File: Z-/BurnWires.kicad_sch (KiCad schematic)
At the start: 27 parts, among them K1 IM02DGR, Q11 IRLML2803, Q13 IRLML2803, Q15 IRF7404, Q17 IRF7404, Q18 IRLML2803, Q19 IRF7404, Q9 MMBT2222AT

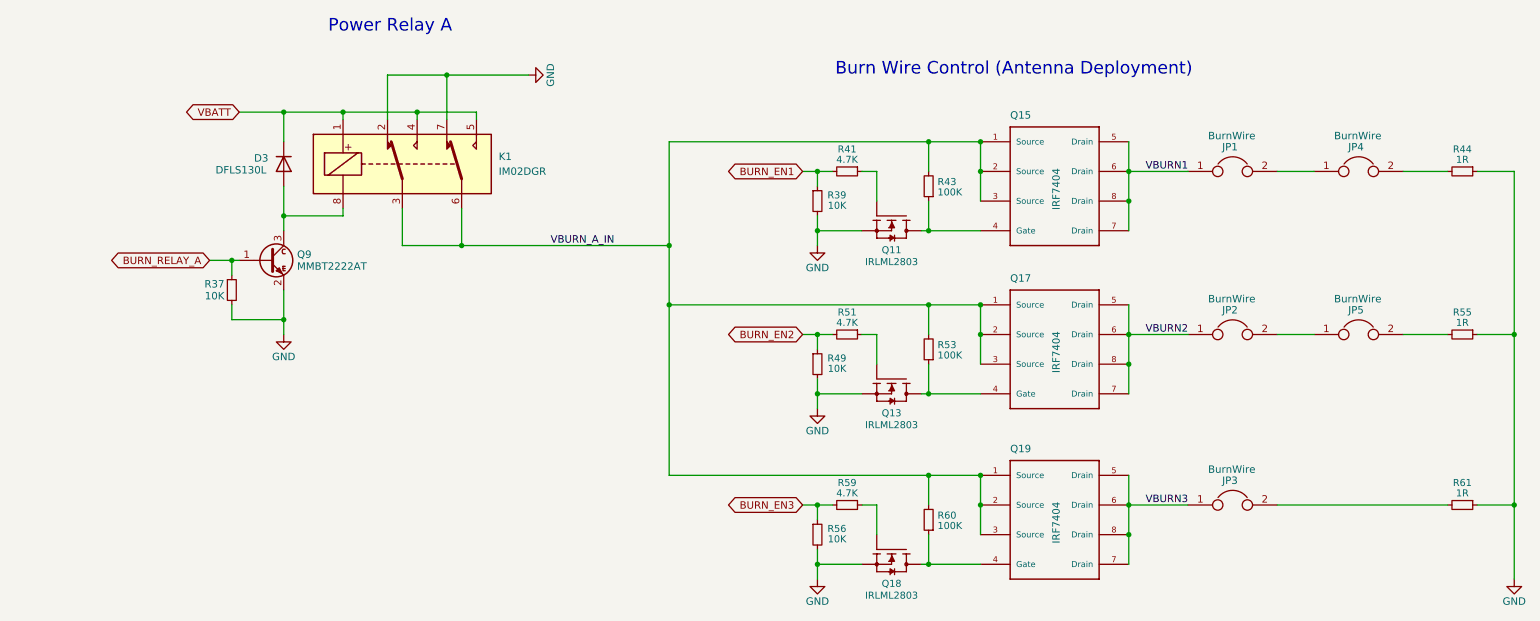
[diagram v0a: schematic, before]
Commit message: Added i2c expander for burnwires, reformatted i2c protection, swapped to drv8235
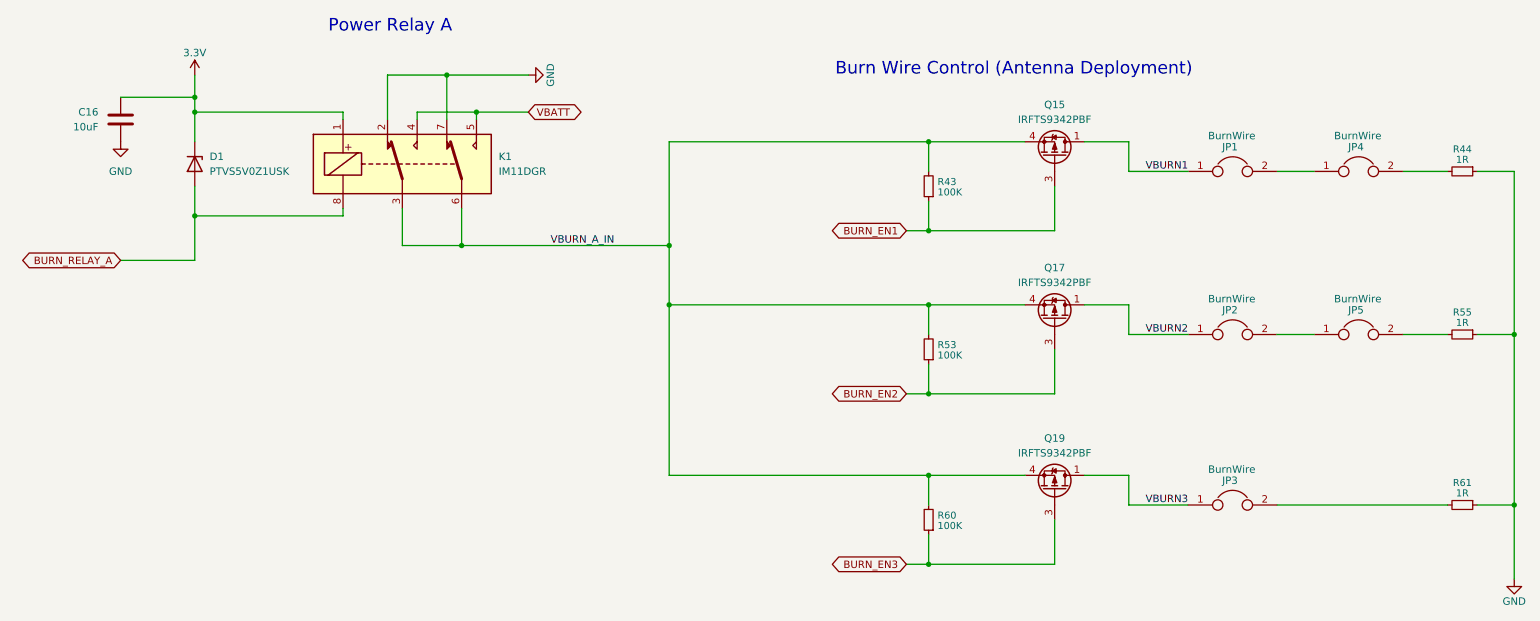
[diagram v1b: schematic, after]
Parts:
- removed D3: DFLS130L, Diode_SMD:D_PowerDI-123, symbol SolarPanels:D
- removed Q11, Q13, Q18: IRLML2803, Package_TO_SOT_SMD:SOT-23, symbol SolarPanels:IRLML2803TRPBF
- removed Q15, Q17, Q19: IRF7404, Package_SO:SOIC-8_3.9x4.9mm_P1.27mm, symbol SolarPanels:NDS8434_3
- removed Q9: MMBT2222AT, Package_TO_SOT_SMD:SOT-23, symbol SolarPanels:MMBT2222AT
- removed R37, R39, R49, R56: 10K, Resistor_SMD:R_0603_1608Metric, symbol SolarPanels:R_Small
- removed R41, R51, R59: 4.7K, Resistor_SMD:R_0603_1608Metric, symbol SolarPanels:R_Small
- added C16: 10uF, Capacitor_SMD:C_1206_3216Metric, symbol Device:C
- added D1: PTVS5V0Z1USK, Diode_SMD:Nexperia_DSN1608-2_1.6x0.8mm, symbol Diode:PTVS5V0Z1USK
- added Q15, Q17, Q19: IRFTS9342PBF, Package_SO:TSOP-6_1.65x3.05mm_P0.95mm, symbol Transistor_FET:IRFTS9342PBF
- K1: value IM02DGR -> IM11DGR
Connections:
- net BURN_EN1: now also R43.1, Q15.3 (G)
- net BURN_EN2: now also R53.1, Q17.3 (G)
- net BURN_EN3: now also R60.1, Q19.3 (G)
- net BURN_RELAY_A: now also K1.8, D1.2 (A)
- net GND: now also C16.2
- net VBATT: no longer K1.1
- net VBURN1: now also Q15.1 (D), Q15.2 (D), Q15.5 (D), Q15.6 (D)
- net VBURN2: now also Q17.1 (D), Q17.2 (D), Q17.5 (D), Q17.6 (D)
- net VBURN3: now also Q19.1 (D), Q19.2 (D), Q19.5 (D), Q19.6 (D)
- net VBURN_A_IN: now also Q15.4 (S), Q17.4 (S), Q19.4 (S)
- new net 3.3V: C16.1, D1.1 (K), K1.1

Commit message: Moved burnwire around and added switch to coil driver
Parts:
- JP1, JP2, JP3, JP4, JP5: footprint SolarPanels:Burn-Wire -> Argus-Miscellaneous:Burn-Wire; symbol SolarPanels:Device_Jumper -> SP:Device_Jumper
- K1: symbol SolarPanels:IM02 -> Relay:IM02
- R43, R44, R53, R55, R60, R61: symbol SolarPanels:R_Small -> Device:R_Small
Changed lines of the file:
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@@
 	)
 	(symbol
-		(lib_id "SolarPanels:R_Small")
+		(lib_id "Device:R_Small")
 		(at 177.8 101.6 180)
 		(unit 1)
@@
 	)
 	(symbol
-		(lib_id "SolarPanels:Device_Jumper")
+		(lib_id "SP:Device_Jumper")
 		(at 251.46 71.12 0)
 		(unit 1)
@@
 			)
 		)
-		(property "Footprint" "SolarPanels:Burn-Wire"
+		(property "Footprint" "Argus-Miscellaneous:Burn-Wire"
 			(at 251.46 71.12 0)
 			(effects
@@
 	)
 	(symbol
-		(lib_id "SolarPanels:Device_Jumper")
+		(lib_id "SP:Device_Jumper")
 		(at 229.87 99.06 0)
 		(unit 1)
@@
 			)
 		)
-		(property "Footprint" "SolarPanels:Burn-Wire"
+		(property "Footprint" "Argus-Miscellaneous:Burn-Wire"
 			(at 229.87 99.06 0)
 			(effects
@@
 	)
 	(symbol
-		(lib_id "SolarPanels:Device_Jumper")
+		(lib_id "SP:Device_Jumper")
 		(at 251.46 99.06 0)
 		(unit 1)
@@
 			)
 		)
-		(property "Footprint" "SolarPanels:Burn-Wire"
+		(property "Footprint" "Argus-Miscellaneous:Burn-Wire"
 			(at 251.46 99.06 0)
 			(effects
@@
 	)
 	(symbol
-		(lib_id "SolarPanels:R_Small")
+		(lib_id "Device:R_Small")
 		(at 269.24 71.12 270)
 		(unit 1)
@@
 	)
 	(symbol
-		(lib_id "SolarPanels:IM02")
+		(lib_id "Relay:IM02")
 		(at 87.63 69.85 0)
 		(unit 1)
@@
 	)
 	(symbol
-		(lib_id "SolarPanels:R_Small")
+		(lib_id "Device:R_Small")
 		(at 269.24 128.27 270)
 		(unit 1)
@@
 	)
 	(symbol
-		(lib_id "SolarPanels:R_Small")
+		(lib_id "Device:R_Small")
 		(at 177.8 73.66 180)
 		(unit 1)
@@
 	)
 	(symbol
-		(lib_id "SolarPanels:R_Small")
+		(lib_id "Device:R_Small")
 		(at 177.8 130.81 180)
 		(unit 1)
@@
 	)
 	(symbol
-		(lib_id "SolarPanels:Device_Jumper")
+		(lib_id "SP:Device_Jumper")
 		(at 229.87 71.12 0)
 		(unit 1)
@@
 			)
 		)
-		(property "Footprint" "SolarPanels:Burn-Wire"
+		(property "Footprint" "Argus-Miscellaneous:Burn-Wire"
 			(at 229.87 71.12 0)
 			(effects
@@
 	)
 	(symbol
-		(lib_id "SolarPanels:R_Small")
+		(lib_id "Device:R_Small")
 		(at 269.24 99.06 270)
 		(unit 1)
@@
 	)
 	(symbol
-		(lib_id "SolarPanels:Device_Jumper")
+		(lib_id "SP:Device_Jumper")
 		(at 229.87 128.27 0)
 		(unit 1)
@@
 			)
 		)
-		(property "Footprint" "SolarPanels:Burn-Wire"
+		(property "Footprint" "Argus-Miscellaneous:Burn-Wire"
 			(at 229.87 128.27 0)
 			(effects

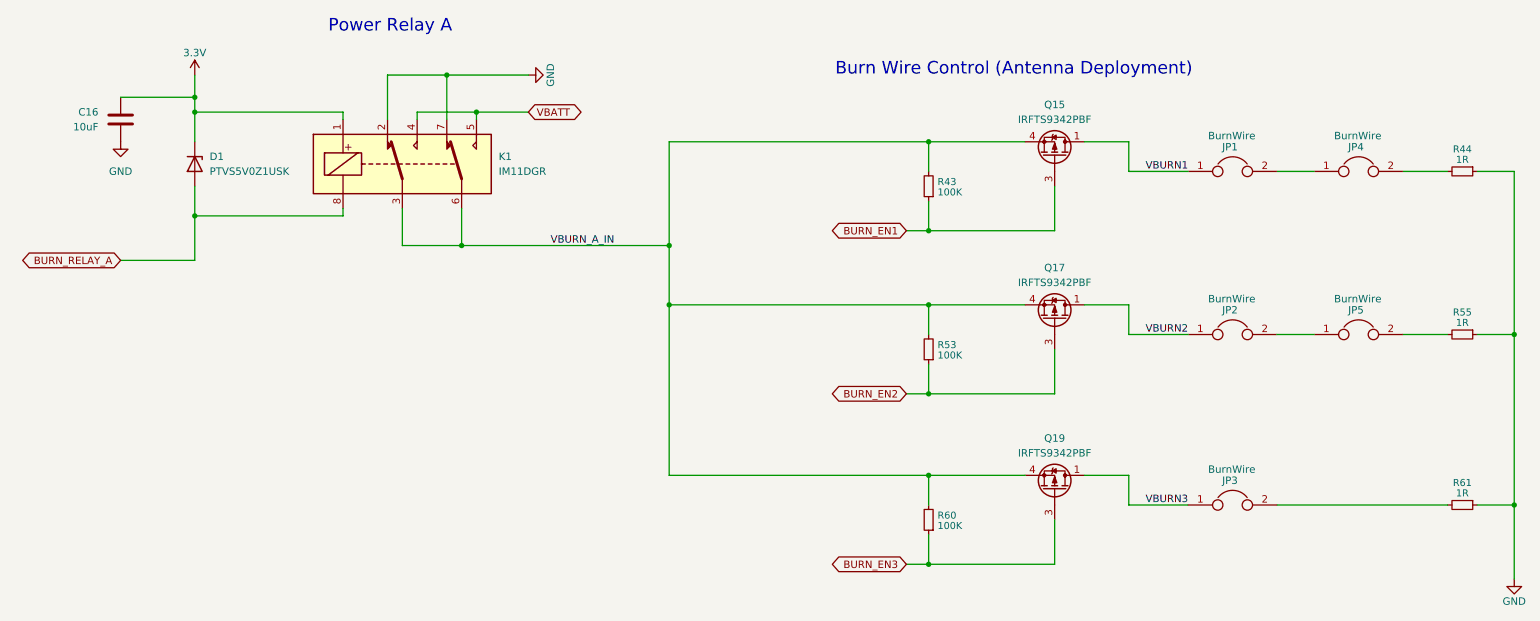
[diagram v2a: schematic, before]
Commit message: Started adding main/peripheral 3v3 nets
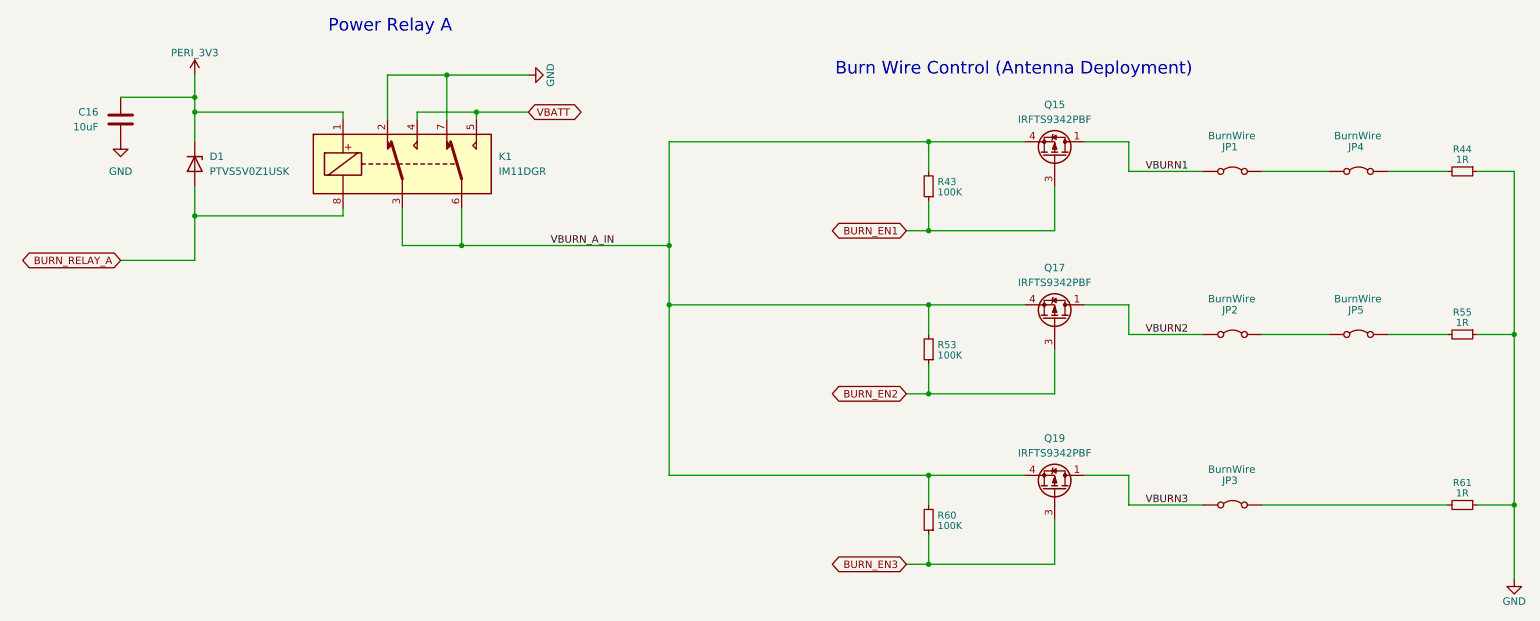
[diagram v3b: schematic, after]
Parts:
- JP1, JP2, JP3, JP4, JP5: symbol SP:Device_Jumper -> Jumper:Jumper_2_Bridged
- K1: footprint SolarPanels:RELAY8_SMTGUL_TEC -> Argus-Miscellaneous:RELAY8_SMTGUL_TEC
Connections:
- net 3.3V renamed PERI_3V3
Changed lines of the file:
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@@
+	(wire
+		(pts
+			(xy 234.95 128.27) (xy 266.7 128.27)
+		)
+		(stroke
+			(width 0)
+			(type default)
+		)
+	)
 	(wire
 		(pts
@@
 	(wire
 		(pts
-			(xy 259.08 99.06) (xy 266.7 99.06)
-		)
-		(stroke
-			(width 0)
-			(type default)
-		)
-	)
-	(wire
-		(pts
 			(xy 177.8 93.98) (xy 194.31 93.98)
 		)
@@
 	(wire
 		(pts
+			(xy 234.95 99.06) (xy 246.38 99.06)
+		)
+		(stroke
+			(width 0)
+			(type default)
+		)
+	)
+	(wire
+		(pts
 			(xy 95.25 54.61) (xy 109.22 54.61)
 		)
@@
 	(wire
 		(pts
-			(xy 212.09 71.12) (xy 222.25 71.12)
+			(xy 212.09 71.12) (xy 224.79 71.12)
 		)
 		(stroke
@@
 	(wire
 		(pts
-			(xy 259.08 71.12) (xy 266.7 71.12)
-		)
-		(stroke
-			(width 0)
-			(type default)
-		)
-	)
-	(wire
-		(pts
 			(xy 278.13 71.12) (xy 278.13 99.06)
 		)
@@
 	(wire
 		(pts
-			(xy 212.09 128.27) (xy 222.25 128.27)
+			(xy 212.09 128.27) (xy 224.79 128.27)
 		)
 		(stroke
@@
 	(wire
 		(pts
-			(xy 237.49 99.06) (xy 243.84 99.06)
-		)
-		(stroke
-			(width 0)
-			(type default)
-		)
-	)
-	(wire
-		(pts
 			(xy 278.13 140.97) (xy 278.13 128.27)
 		)
@@
 	(wire
 		(pts
+			(xy 256.54 99.06) (xy 266.7 99.06)
+		)
+		(stroke
+			(width 0)
+			(type default)
+		)
+	)
+	(wire
+		(pts
 			(xy 173.99 81.28) (xy 177.8 81.28)
 		)
@@
 	(wire
 		(pts
-			(xy 212.09 99.06) (xy 222.25 99.06)
+			(xy 212.09 99.06) (xy 224.79 99.06)
 		)
 		(stroke
@@
 	(wire
 		(pts
-			(xy 237.49 71.12) (xy 243.84 71.12)
-		)
-		(stroke
-			(width 0)
-			(type default)
-		)
-	)
-	(wire
-		(pts
 			(xy 52.07 78.74) (xy 77.47 78.74)
 		)
@@
 	(wire
 		(pts
+			(xy 234.95 71.12) (xy 246.38 71.12)
+		)
+		(stroke
+			(width 0)
+			(type default)
+		)
+	)
+	(wire
+		(pts
 			(xy 173.99 138.43) (xy 177.8 138.43)
 		)
@@
 	(wire
 		(pts
-			(xy 237.49 128.27) (xy 266.7 128.27)
-		)
-		(stroke
-			(width 0)
-			(type default)
-		)
-	)
-	(wire
-		(pts
 			(xy 85.09 54.61) (xy 95.25 54.61)
 		)
@@
 		(pts
 			(xy 204.47 123.19) (xy 212.09 123.19)
+		)
+		(stroke
+			(width 0)
+			(type default)
+		)
+	)
+	(wire
+		(pts
+			(xy 256.54 71.12) (xy 266.7 71.12)
 		)
 		(stroke
@@
 	)
 	(symbol
-		(lib_id "SP:Device_Jumper")
+		(lib_id "Jumper:Jumper_2_Bridged")
 		(at 251.46 71.12 0)
 		(unit 1)
@@
 	)
 	(symbol
-		(lib_id "SP:Device_Jumper")
+		(lib_id "Jumper:Jumper_2_Bridged")
 		(at 229.87 99.06 0)
 		(unit 1)
@@
 	)
 	(symbol
-		(lib_id "SP:Device_Jumper")
+		(lib_id "Jumper:Jumper_2_Bridged")
 		(at 251.46 99.06 0)
 		(unit 1)
@@
 			)
 		)
-		(property "Footprint" "SolarPanels:RELAY8_SMTGUL_TEC"
+		(property "Footprint" "Argus-Miscellaneous:RELAY8_SMTGUL_TEC"
 			(at 87.63 69.85 0)
 			(effects
@@
 	)
 	(symbol
-		(lib_id "SP:Device_Jumper")
+		(lib_id "Jumper:Jumper_2_Bridged")
 		(at 229.87 71.12 0)
 		(unit 1)
@@
 			)
 		)
-		(property "Value" "3.3V"
+		(property "Value" "PERI_3V3"
 			(at 52.07 50.8 0)
 			(effects
@@
 	)
 	(symbol
-		(lib_id "SP:Device_Jumper")
+		(lib_id "Jumper:Jumper_2_Bridged")
 		(at 229.87 128.27 0)
 		(unit 1)

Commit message: Updated schematics/layout with mainboard compatability
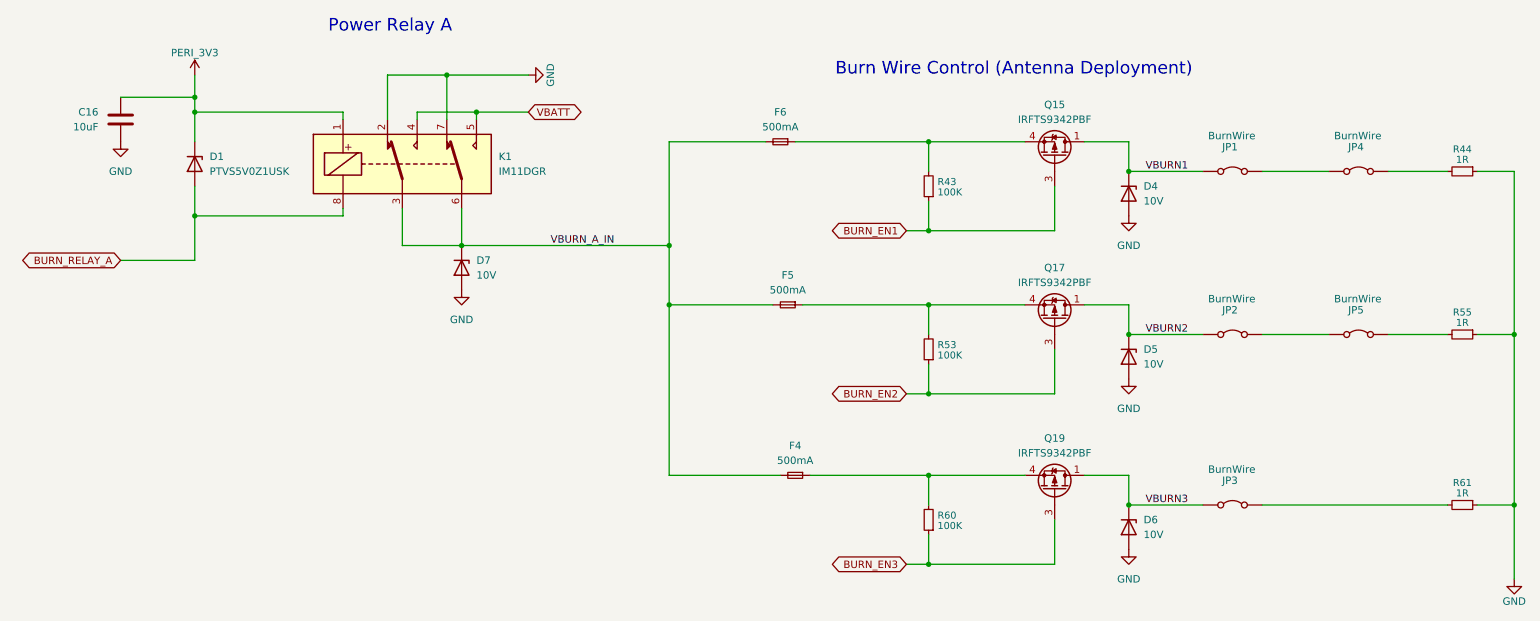
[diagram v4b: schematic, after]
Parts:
- added D4, D5, D6, D7: 10V, Diode_SMD:Nexperia_DSN1608-2_1.6x0.8mm, symbol Diode:PTVS10VZ1USK
- added F4, F5, F6: 500mA, Fuse:Fuse_0603_1608Metric, symbol Device:Fuse_Small
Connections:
- net GND: now also D4.2 (A), D5.2 (A), D6.2 (A), D7.2 (A)
- net VBURN1: now also D4.1 (K)
- net VBURN2: now also D5.1 (K)
- net VBURN3: now also D6.1 (K)
- net VBURN_A_IN: now also D7.1 (K), F4.2, F5.2, F6.2; no longer Q15.4 (S), Q17.4 (S), Q19.4 (S), R43.2, R53.2, R60.2
- new net: F5.1, Q17.4 (S), R53.2
- new net: F4.1, Q19.4 (S), R60.2
- new net: F6.1, Q15.4 (S), R43.2
